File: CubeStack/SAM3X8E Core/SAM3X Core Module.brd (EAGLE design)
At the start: 76.2 x 76.2 mm, 53 parts, among them CN1 100nF, CN2 100nF, CN3 100nF, CN4 100nF, IC1 SAM3X8E(ARDUINO), Q1 MBT3904DW2T1, Q2 MBT3904DW2T1, X1 16POS_RIBBON, X2 16POS_RIBBON, X3 16POS_RIBBON, X4 16POS_RIBBON, Y1 FH1200001, Y2 ABS05

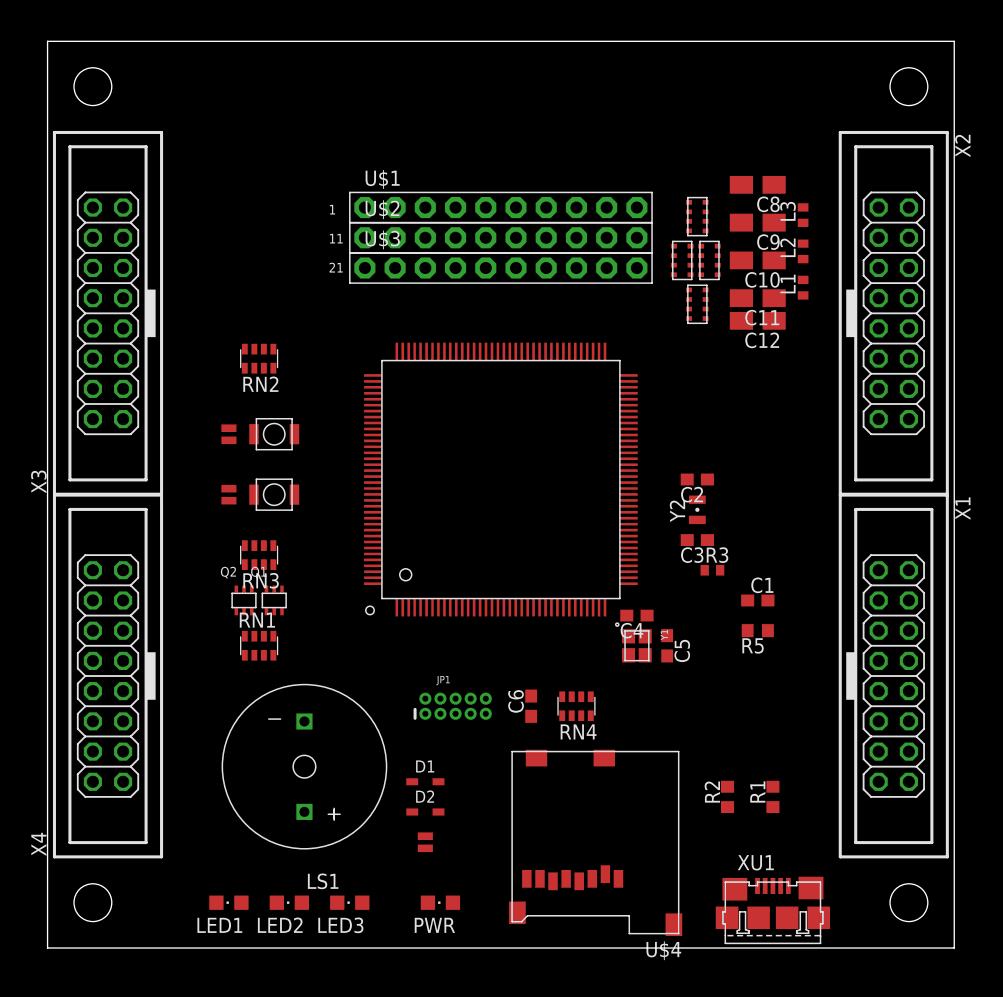
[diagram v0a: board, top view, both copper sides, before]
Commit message: First Draft of SAM3X CPU Core
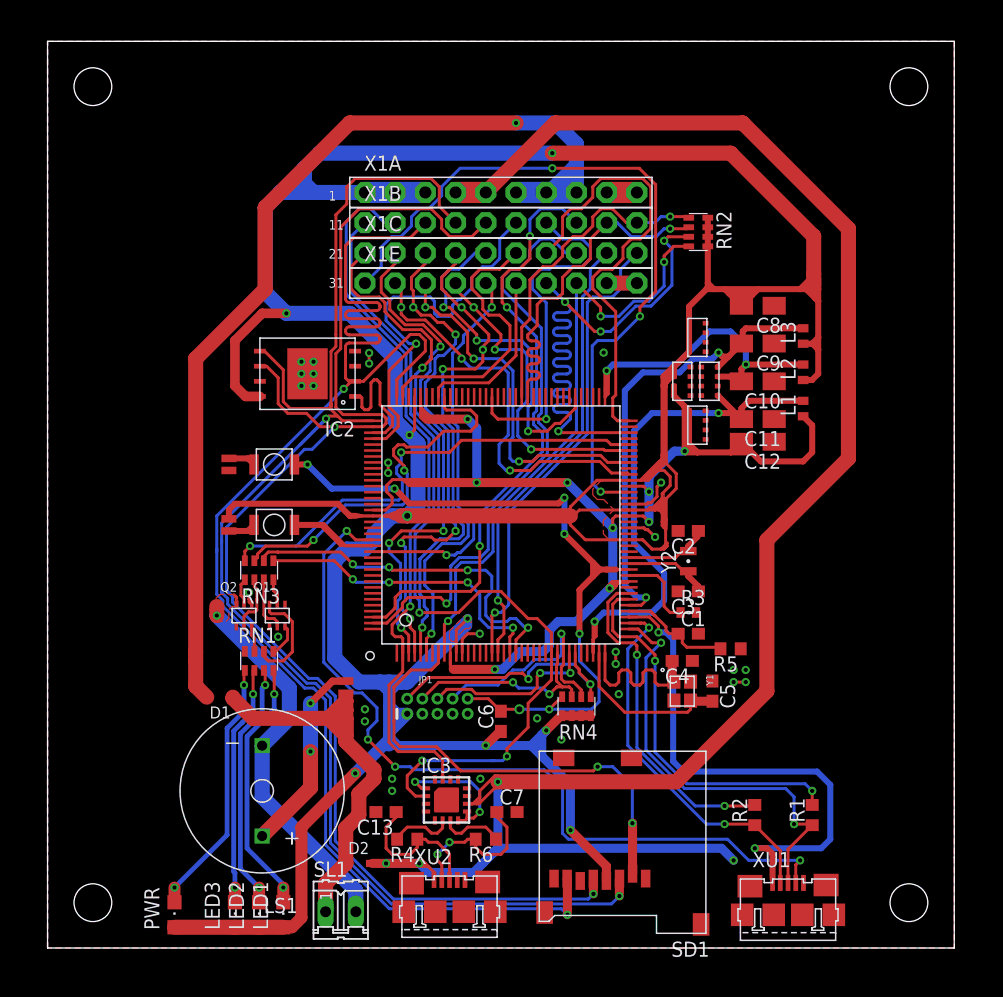
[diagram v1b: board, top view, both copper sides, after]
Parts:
- removed U$1, U$2, U$3: PINHD-1X10, adafruit:1X10-BIG
- removed U$4: MICROSD, CPSS_CONNECTOR:CONN_MICROSD
- removed X1, X2, X3, X4: 16POS_RIBBON, CPSS_CONNECTOR:2X08
- added C13, C7: (no value), resistor:C0603
- added IC2: W25QXXDV, CPSS_IC:WSON
- added IC3: FT230XQ, ftdichip:QFN16
- added R4, R6: (no value), resistor:R0603
- added SD1: MICROSD, CPSS_CONNECTOR:CONN_MICROSD
- added SL1: (no value), con-amp-quick:02P
- added X1A, X1B, X1C, X1E: PINHD-1X10, adafruit:1X10-BIG
- added XU2: MICROUSB_5POS_SMT, CPSS_CONNECTOR:RECPT_SMT_R/A
- moved RN2 38.4 mm to (54.7, 60.2), turned to 270 degrees
- moved PWR 22.4 mm to (10.7, 2.79), turned to 0 degrees
- moved D1 18.7 mm to (14.5, 21.1), turned to 180 degrees
- moved SJ1 14.6 mm to (25.1, 21.9), turned to 0 degrees
- moved C8 10.2 mm to (59.7, 54.0)
- moved C9 10.2 mm to (59.7, 50.8)
- moved CN4 10.2 mm to (54.6, 51.3)
- moved L1 10.2 mm to (63.5, 45.3)
- moved C10 10.2 mm to (59.7, 47.6)
- moved C11 10.2 mm to (59.7, 44.5)
- moved C12 10.2 mm to (59.7, 42.5)
- moved CN1 10.2 mm to (53.3, 47.6)
- moved CN2 10.2 mm to (55.6, 47.6)
- moved CN3 10.2 mm to (54.6, 43.9)
- moved L2 10.2 mm to (63.5, 48.4)
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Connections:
- net D+ renamed D+0
- net D- renamed D-0
- net LS_DRIVE_R renamed N$1
- net N$32 renamed XCK_N
- net N$34 renamed XCK_P
- removed net A0: IC1.P$78, X1.15
- removed net AREF: X1.14, X2.14, X3.14, X4.14
- removed net D2: IC1.P$144, X2.13
- removed net NPCS2/52: U$2.3
- removed net RTS1: U$2.8
- removed net RTS2: U$3.2
- removed net RX/D0: IC1.P$27, U$1.5, X2.11
- removed net TX/D1: IC1.P$2, U$1.6, X2.12
- new net 3.3V_FTDI: IC3.1, IC3.8, IC3.9
- new net D+1: C13.1, R4.1, XU2.P3
- new net D-1: C7.1, R6.2, XU2.P2
- new net N$3: IC3.6, R4.2
- new net N$4: IC3.7, R6.1
- new net RX: IC1.P$27, IC3.2, X1B.1
- new net SD_CS: IC1.P$8, SD1.2
- new net TX: IC1.P$2, IC3.15, X1B.2
- net 3.3V: now also IC2.P8, SD1.4, X1A.1, X1A.2, X1A.3; no longer U$1.1, U$4.4, X1.1, X2.1, X3.1, X4.1
- net 5V: now also IC3.10, X1A.4, X1A.5, XU2.P1; no longer U$1.2
- net A1: no longer X1.16
- net A2: no longer X2.15
- net A3: no longer X2.16
- net A4: no longer X4.15
- net A5: no longer X4.16
- net A6: no longer X3.15
- net A7: no longer X3.16
- net D11: now also RN3.1; no longer RN3.2
- net D12: now also RN3.2; no longer RN3.3
- net D3: no longer X1.11
- net D33: no longer X3.11
- net D34: no longer X3.12
- net D36: no longer X3.13
- net D4: no longer X1.12
- net D46: no longer X4.11
- net D47: no longer X4.12
- net D48: no longer X4.13
- net D5: no longer X1.13
- net GND: now also C13.2, C7.2, IC2.P4, IC2.TH, IC3.13, IC3.3, SD1.6, SD1.GND1, SD1.GND2, SD1.GND3, X1A.10, X1A.9, X1E.10, X1E.9, XU2.P5; no longer U$1.4, U$4.6, U$4.GND1, U$4.GND2, U$4.GND3, X1.2, X2.2, X3.2, X4.2
- net HV: now also X1A.6, X1A.7, X1A.8; no longer U$1.3, X1.3, X2.3, X3.3, X4.3
- net JTAG_TCK: now also RN4.3; no longer RN4.2
- net JTAG_TDI: now also RN4.2; no longer RN4.3
- net LS_D: now also SL1.2
- net LS_DRIVE: now also SL1.1
- net LS_G: now also RN3.6; no longer RN3.8
- net L_1_G: now also RN3.8; no longer RN3.7
- net L_2_G: now also RN3.7; no longer RN3.6
- net MISO: now also IC2.P2, SD1.7, X1B.3; no longer U$1.9, U$4.7, X1.6, X2.6, X3.6, X4.6
- net MOSI: now also IC2.P5, SD1.3, X1B.4; no longer U$1.10, U$4.3, X1.7, X2.7, X3.7, X4.7
- net NPCS0/D10: now also IC2.P1; no longer U$4.2
- net NPCS1/D4: now also X1B.6; no longer U$2.2
- net NPCS2/D52: now also X1B.7
- net NPCS3: now also X1B.8; no longer U$2.4
- net PWM0/D35: now also X1E.1; no longer U$3.5
- net PWM1/D37: now also X1E.2; no longer U$3.6
- net PWM2/D39: now also X1E.3; no longer U$3.7
- net PWM3/D41: now also X1E.4; no longer U$3.8
- net PWM4: now also X1E.5; no longer U$3.9
- net PWM5/D44: now also X1E.6; no longer U$3.10
- net PWM6/D45: now also RN3.3; no longer RN3.1
- net RXD0: now also X1C.1; no longer X2.4
- net RXD1: now also X1C.3; no longer U$2.5, X3.4
- net RXD2: now also X1C.6; no longer U$2.9, X1.4
- net RXD3: now also X1C.9; no longer X4.4
- net SCK: now also IC2.P6, SD1.5, X1B.5; no longer U$2.1, U$4.5, X1.8, X2.8, X3.8, X4.8
- net SCK1: now also IC1.P$78, X1C.5; no longer U$2.7
- net SCK2: now also IC1.P$143, X1C.8; no longer U$3.1
- net SCL: now also X1B.10; no longer U$1.8, X1.10, X2.10, X3.10, X4.10
- net SCL1: now also X1E.7; no longer U$3.4
- net SDA: now also X1B.9; no longer U$1.7, X1.9, X2.9, X3.9, X4.9
- net SDA1: now also X1E.8; no longer U$3.3
- net TXD0: now also X1C.2; no longer X2.5
- net TXD1: now also X1C.4; no longer U$2.6, X3.5
- net TXD2: now also X1C.7; no longer U$2.10, X1.5
- net TXD3: now also X1C.10; no longer X4.5
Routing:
- net 3.3V: track 0.00 -> 384.9 mm, vias 0 -> 9
- net 5V: track 0.00 -> 160.7 mm, vias 0 -> 4
- net MISO: track 0.00 -> 122.8 mm, vias 0 -> 2
- net MOSI: track 0.00 -> 121.4 mm, vias 0 -> 2
- net SCK: track 0.00 -> 118.1 mm, vias 0 -> 2
- net 1.8V: track 0.00 -> 112.5 mm, vias 0 -> 9
- net HV: track 0.00 -> 86.9 mm, vias 0 -> 1
- net RX: track 0.00 -> 74.3 mm, vias 0 -> 3
- net UOTGID: track 0.00 -> 68.2 mm, vias 0 -> 4
- net M_RESET: track 0.00 -> 63.7 mm, vias 0 -> 7
- net PWM0/D35: track 0.00 -> 62.4 mm, vias 0 -> 3
- net TX: track 0.00 -> 61.6 mm, vias 0 -> 1
- net SCL1: track 0.00 -> 52.2 mm, vias 0 -> 4
- net SDA1: track 0.00 -> 51.8 mm, vias 0 -> 3
- net NPCS3: track 0.00 -> 51.2 mm, vias 0 -> 3
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- added copper zone on layer 1, net 3.3V
- added copper zone on layer 1, net 5V
- added copper zone on layer 1, net GND
- added copper zone on layer 16, net GND
- added copper zone on layer 1, net LS_D
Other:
- outline, holes or cut-outs redrawn
- board text added: "1 11 21 31"
- board text removed: "1 11 21"

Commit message: Modified Libraries, Worked on STM32F3 Core
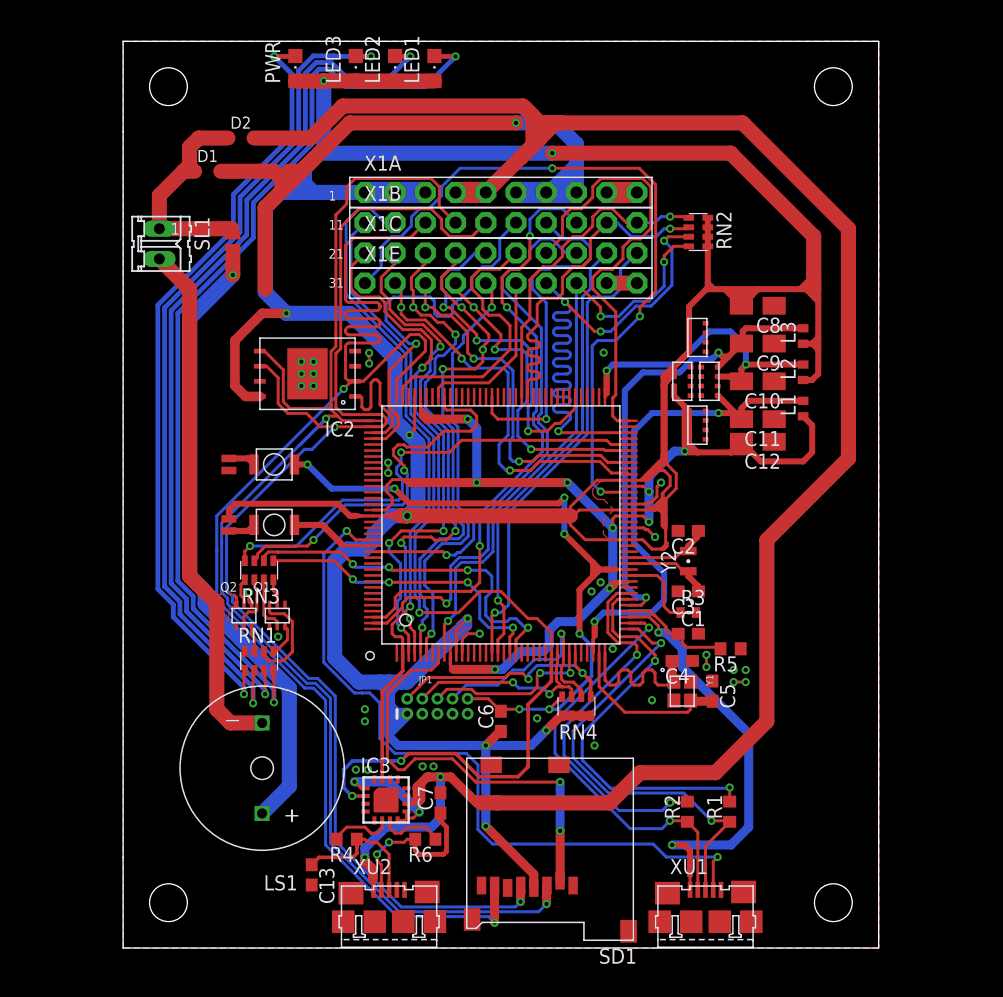
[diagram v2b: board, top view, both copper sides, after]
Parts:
- moved LED1 72.2 mm to (32.5, 73.9)
- moved LED2 72.0 mm to (29.2, 73.9)
- moved LED3 71.8 mm to (25.9, 73.9)
- moved PWR 71.8 mm to (20.8, 73.9)
- moved D2 61.8 mm to (16.3, 68.1)
- moved SL1 58.2 mm to (9.40, 59.2), turned to 270 degrees
- moved D1 44.2 mm to (13.5, 65.3), turned to 0 degrees
- moved SJ1 38.6 mm to (15.6, 59.4), turned to 180 degrees
- moved C13 8.18 mm to (22.2, 6.15), turned to 270 degrees
- moved XU1 6.96 mm to (55.3, 2.21)
- moved R1 6.94 mm to (57.3, 11.5)
- moved SD1 6.12 mm to (49.5, 16.0)
- moved R2 5.67 mm to (53.8, 11.5)
- moved C7 5.64 mm to (33.0, 12.2), turned to 90 degrees
- moved XU2 5.15 mm to (28.7, 2.21)
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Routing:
- net L_1: track 21.7 -> 79.3 mm
- net L_2: track 21.0 -> 74.8 mm
- net L_3: track 20.3 -> 71.7 mm
- net L_PWR_D: track 21.9 -> 65.7 mm
- net N$1: track 16.6 -> 53.5 mm, vias 2 -> 1
- net HV: track 86.9 -> 60.5 mm
- net LS_DRIVE: track 37.1 -> 19.1 mm
- net 5V: track 160.7 -> 177.1 mm, vias 4 -> 2
- net 3.3V: track 384.9 -> 368.8 mm
- net LS_D: track 34.0 -> 46.5 mm, vias 1 -> 0
- net VBUS: track 44.5 -> 35.3 mm
- net RX: track 74.3 -> 83.1 mm
- net UOTGID: track 68.2 -> 62.1 mm, vias 4 -> 2
- net MISO: track 122.8 -> 117.0 mm
- net MOSI: track 121.4 -> 115.6 mm
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- removed copper zone on layer 1, net 5V
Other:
- board size 76.2 x 76.2 mm -> 63.5 x 76.2 mm
